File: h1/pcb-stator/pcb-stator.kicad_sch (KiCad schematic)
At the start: 1 part, among them J1 Conn_01x01_Pin

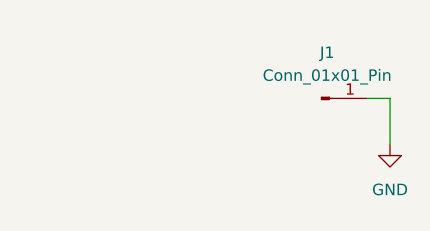
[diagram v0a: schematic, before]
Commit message: h1: fixed stator alignment
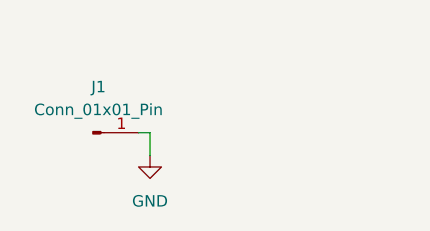
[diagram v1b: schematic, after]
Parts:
- J1: footprint Connector_Wire:SolderWirePad_1x01_SMD_3x6mm -> Connector_Wire:SolderWirePad_1x01_SMD_1x2mm
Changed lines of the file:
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@@
 	(wire
 		(pts
-			(xy 102.87 91.44) (xy 102.87 96.52)
+			(xy 76.2 95.25) (xy 76.2 97.79)
 		)
 		(stroke
@@
 	(wire
 		(pts
-			(xy 100.33 91.44) (xy 102.87 91.44)
+			(xy 74.93 95.25) (xy 76.2 95.25)
 		)
 		(stroke
@@
 	)
 	(symbol
-		(lib_id "power:GND")
-		(at 102.87 96.52 0)
+		(lib_id "Connector:Conn_01x01_Pin")
+		(at 69.85 95.25 0)
 		(unit 1)
 		(exclude_from_sim no)
@@
 		(dnp no)
 		(fields_autoplaced yes)
-		(property "Reference" "#PWR01"
-			(at 102.87 102.87 0)
+		(property "Reference" "J1"
+			(at 70.485 90.17 0)
+			(effects
+				(font
+					(size 1.27 1.27)
+				)
+			)
+		)
+		(property "Value" "Conn_01x01_Pin"
+			(at 70.485 92.71 0)
+			(effects
+				(font
+					(size 1.27 1.27)
+				)
+			)
+		)
+		(property "Footprint" "Connector_Wire:SolderWirePad_1x01_SMD_1x2mm"
+			(at 69.85 95.25 0)
 			(effects
 				(font
@@
 			)
 		)
-		(property "Value" "GND"
-			(at 102.87 101.6 0)
-			(effects
-				(font
-					(size 1.27 1.27)
-				)
-			)
-		)
-		(property "Footprint" ""
-			(at 102.87 96.52 0)
+		(property "Datasheet" "~"
+			(at 69.85 95.25 0)
 			(effects
 				(font
@@
 			)
 		)
-		(property "Datasheet" ""
-			(at 102.87 96.52 0)
-			(effects
-				(font
-					(size 1.27 1.27)
-				)
-				(hide yes)
-			)
-		)
-		(property "Description" "Power symbol creates a global label with name \"GND\" , ground"
-			(at 102.87 96.52 0)
+		(property "Description" "Generic connector, single row, 01x01, script generated"
+			(at 69.85 95.25 0)
 			(effects
 				(font
@@
 		(instances
 			(project ""
-				(path "/1495eec9-70a9-4ebf-8286-8409dbfa864b"
-					(reference "#PWR01")
+				(path "/f4431aee-b232-4205-b25a-cd690a77edaa"
+					(reference "J1")
 					(unit 1)
 				)
@@
 	)
 	(symbol
-		(lib_id "Connector:Conn_01x01_Pin")
-		(at 95.25 91.44 0)
+		(lib_id "power:GND")
+		(at 76.2 97.79 0)
 		(unit 1)
 		(exclude_from_sim no)
@@
 		(dnp no)
 		(fields_autoplaced yes)
-		(property "Reference" "J1"
-			(at 95.885 86.36 0)
-			(effects
-				(font
-					(size 1.27 1.27)
-				)
-			)
-		)
-		(property "Value" "Conn_01x01_Pin"
-			(at 95.885 88.9 0)
-			(effects
-				(font
-					(size 1.27 1.27)
-				)
-			)
-		)
-		(property "Footprint" "Connector_Wire:SolderWirePad_1x01_SMD_3x6mm"
-			(at 95.25 91.44 0)
+		(property "Reference" "#PWR01"
+			(at 76.2 104.14 0)
 			(effects
 				(font
@@
 			)
 		)
-		(property "Datasheet" "~"
-			(at 95.25 91.44 0)
+		(property "Value" "GND"
+			(at 76.2 102.87 0)
+			(effects
+				(font
+					(size 1.27 1.27)
+				)
+			)
+		)
+		(property "Footprint" ""
+			(at 76.2 97.79 0)
 			(effects
 				(font
@@
 			)
 		)
-		(property "Description" "Generic connector, single row, 01x01, script generated"
-			(at 95.25 91.44 0)
+		(property "Datasheet" ""
+			(at 76.2 97.79 0)
+			(effects
+				(font
+					(size 1.27 1.27)
+				)
+				(hide yes)
+			)
+		)
+		(property "Description" "Power symbol creates a global label with name \"GND\" , ground"
+			(at 76.2 97.79 0)
 			(effects
 				(font
@@
 		(instances
 			(project ""
-				(path "/1495eec9-70a9-4ebf-8286-8409dbfa864b"
-					(reference "J1")
+				(path "/f4431aee-b232-4205-b25a-cd690a77edaa"
+					(reference "#PWR01")
 					(unit 1)
 				)

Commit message: h1: fixed stator & spacer edge cuts
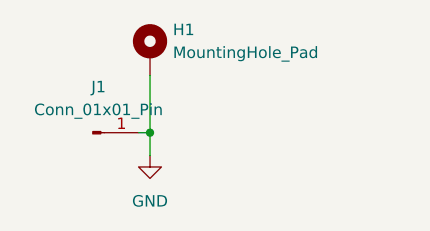
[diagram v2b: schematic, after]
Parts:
- added H1: MountingHole_Pad, MountingHole:MountingHole_2.2mm_M2_DIN965_Pad, symbol Mechanical:MountingHole_Pad
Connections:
- net GND: now also H1.1
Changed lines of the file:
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@@
 	(generator_version "9.0")
 	(paper "A4")
+	(junction
+		(at 76.2 95.25)
+		(diameter 0)
+		(color 0 0 0 0)
+	)
+	(wire
+		(pts
+			(xy 76.2 88.9) (xy 76.2 95.25)
+		)
+		(stroke
+			(width 0)
+			(type default)
+		)
+	)
 	(wire
 		(pts
@@
 					(unit 1)
 				)
+			)
+		)
+	)
+	(symbol
+		(lib_id "Mechanical:MountingHole_Pad")
+		(at 76.2 86.36 0)
+		(unit 1)
+		(exclude_from_sim no)
+		(in_bom no)
+		(on_board yes)
+		(dnp no)
+		(fields_autoplaced yes)
+		(property "Reference" "H1"
+			(at 78.74 83.8199 0)
+			(effects
+				(font
+					(size 1.27 1.27)
+				)
+				(justify left)
+			)
+		)
+		(property "Value" "MountingHole_Pad"
+			(at 78.74 86.3599 0)
+			(effects
+				(font
+					(size 1.27 1.27)
+				)
+				(justify left)
+			)
+		)
+		(property "Footprint" "MountingHole:MountingHole_2.2mm_M2_DIN965_Pad"
+			(at 76.2 86.36 0)
+			(effects
+				(font
+					(size 1.27 1.27)
+				)
+				(hide yes)
+			)
+		)
+		(property "Datasheet" "~"
+			(at 76.2 86.36 0)
+			(effects
+				(font
+					(size 1.27 1.27)
+				)
+				(hide yes)
+			)
+		)
+		(property "Description" "Mounting Hole with connection"
+			(at 76.2 86.36 0)
+			(effects
+				(font
+					(size 1.27 1.27)
+				)
+				(hide yes)
+			)
+		)
+		(pin "1"
+		)
+		(instances
+			(project ""
+				(path "/f4431aee-b232-4205-b25a-cd690a77edaa"
+					(reference "H1")
+					(unit 1)
+				)
